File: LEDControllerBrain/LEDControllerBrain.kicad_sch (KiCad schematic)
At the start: 10 parts, among them J1 TB001-500-04BE, J2 TB001-500-04BE, J3 TB001-500-04BE, U1 NODEMCU-32S

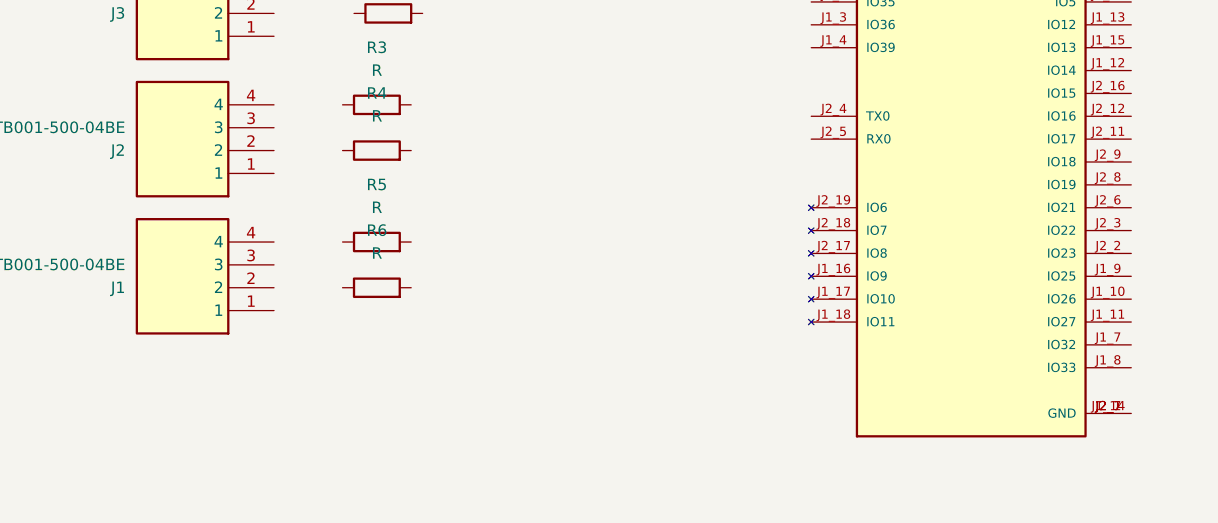
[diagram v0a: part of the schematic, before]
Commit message: add 24v support and reverse voltage protection
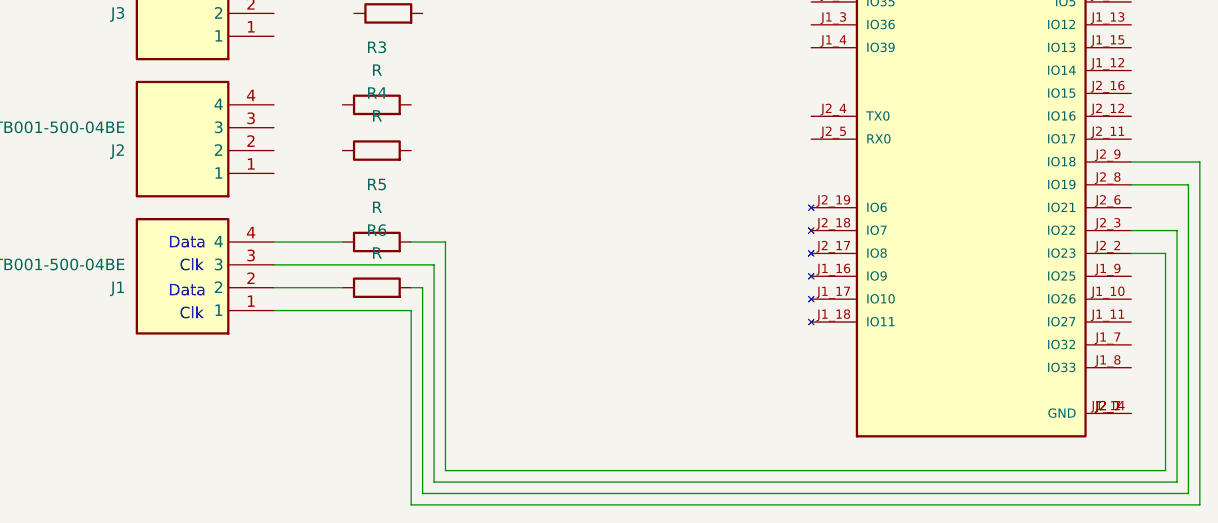
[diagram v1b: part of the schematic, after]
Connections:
- net at R6.1: now also J1.2
- net at R6.2: now also U1.J2_8 (IO19)
- net at J1.1: now also U1.J2_9 (IO18)
- net at J1.3: now also U1.J2_3 (IO22)
- net at J1.4: now also R5.1
- net at U1.J2_2 (IO23): now also R5.2
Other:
- note added: "Clk"
- note added: "Data"
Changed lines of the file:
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@@
 	(generator_version "8.0")
 	(paper "A4")
+	(wire
+		(pts
+			(xy 72.39 82.55) (xy 72.39 106.68)
+		)
+		(stroke
+			(width 0)
+			(type default)
+		)
+	)
+	(wire
+		(pts
+			(xy 157.48 71.12) (xy 149.86 71.12)
+		)
+		(stroke
+			(width 0)
+			(type default)
+		)
+	)
+	(wire
+		(pts
+			(xy 72.39 106.68) (xy 154.94 106.68)
+		)
+		(stroke
+			(width 0)
+			(type default)
+		)
+	)
+	(wire
+		(pts
+			(xy 156.21 107.95) (xy 156.21 73.66)
+		)
+		(stroke
+			(width 0)
+			(type default)
+		)
+	)
+	(wire
+		(pts
+			(xy 156.21 73.66) (xy 149.86 73.66)
+		)
+		(stroke
+			(width 0)
+			(type default)
+		)
+	)
+	(wire
+		(pts
+			(xy 73.66 105.41) (xy 153.67 105.41)
+		)
+		(stroke
+			(width 0)
+			(type default)
+		)
+	)
+	(wire
+		(pts
+			(xy 71.12 107.95) (xy 156.21 107.95)
+		)
+		(stroke
+			(width 0)
+			(type default)
+		)
+	)
+	(wire
+		(pts
+			(xy 72.39 82.55) (xy 54.61 82.55)
+		)
+		(stroke
+			(width 0)
+			(type default)
+		)
+	)
+	(wire
+		(pts
+			(xy 153.67 81.28) (xy 153.67 105.41)
+		)
+		(stroke
+			(width 0)
+			(type default)
+		)
+	)
+	(wire
+		(pts
+			(xy 154.94 78.74) (xy 154.94 106.68)
+		)
+		(stroke
+			(width 0)
+			(type default)
+		)
+	)
+	(wire
+		(pts
+			(xy 69.85 87.63) (xy 69.85 109.22)
+		)
+		(stroke
+			(width 0)
+			(type default)
+		)
+	)
+	(wire
+		(pts
+			(xy 149.86 81.28) (xy 153.67 81.28)
+		)
+		(stroke
+			(width 0)
+			(type default)
+		)
+	)
+	(wire
+		(pts
+			(xy 157.48 109.22) (xy 157.48 71.12)
+		)
+		(stroke
+			(width 0)
+			(type default)
+		)
+	)
+	(wire
+		(pts
+			(xy 54.61 80.01) (xy 62.23 80.01)
+		)
+		(stroke
+			(width 0)
+			(type default)
+		)
+	)
+	(wire
+		(pts
+			(xy 71.12 85.09) (xy 71.12 107.95)
+		)
+		(stroke
+			(width 0)
+			(type default)
+		)
+	)
+	(wire
+		(pts
+			(xy 69.85 85.09) (xy 71.12 85.09)
+		)
+		(stroke
+			(width 0)
+			(type default)
+		)
+	)
+	(wire
+		(pts
+			(xy 69.85 109.22) (xy 157.48 109.22)
+		)
+		(stroke
+			(width 0)
+			(type default)
+		)
+	)
+	(wire
+		(pts
+			(xy 54.61 87.63) (xy 69.85 87.63)
+		)
+		(stroke
+			(width 0)
+			(type default)
+		)
+	)
+	(wire
+		(pts
+			(xy 54.61 85.09) (xy 62.23 85.09)
+		)
+		(stroke
+			(width 0)
+			(type default)
+		)
+	)
+	(wire
+		(pts
+			(xy 154.94 78.74) (xy 149.86 78.74)
+		)
+		(stroke
+			(width 0)
+			(type default)
+		)
+	)
+	(wire
+		(pts
+			(xy 73.66 80.01) (xy 69.85 80.01)
+		)
+		(stroke
+			(width 0)
+			(type default)
+		)
+	)
+	(wire
+		(pts
+			(xy 73.66 105.41) (xy 73.66 80.01)
+		)
+		(stroke
+			(width 0)
+			(type default)
+		)
+	)
+	(text "Data"
+		(exclude_from_sim no)
+		(at 44.958 85.598 0)
+		(effects
+			(font
+				(size 1.27 1.27)
+			)
+		)
+	)
+	(text "Clk"
+		(exclude_from_sim no)
+		(at 45.466 88.138 0)
+		(effects
+			(font
+				(size 1.27 1.27)
+			)
+		)
+	)
+	(text "Clk"
+		(exclude_from_sim no)
+		(at 45.466 82.804 0)
+		(effects
+			(font
+				(size 1.27 1.27)
+			)
+		)
+	)
+	(text "Data"
+		(exclude_from_sim no)
+		(at 44.958 80.264 0)
+		(effects
+			(font
+				(size 1.27 1.27)
+			)
+		)
+	)
 	(symbol
 		(lib_id "Device:R")

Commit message: finished pdb
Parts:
- removed J3: TB001-500-04BE, TB00150004BE, symbol LEDController:TB001-500-04BE
- added R7: R, Resistor_THT:R_Axial_DIN0207_L6.3mm_D2.5mm_P10.16mm_Horizontal, symbol Device:R
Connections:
- net at R4.1: now also J1.4
- net at R4.2: now also U1.J2_14 (IO0)
- net at R6.2: now also U1.J2_9 (IO18); no longer U1.J2_8 (IO19)
- net at R1.1: now also J2.3
- net at R1.2: now also U1.J2_11 (IO17)
- net at R3.1: now also J2.1
- net at R3.2: now also U1.J2_13 (IO4)
- net at J1.1: now also U1.J2_8 (IO19); no longer U1.J2_9 (IO18)
- net at J1.3: now also R5.1; no longer U1.J2_3 (IO22)
- net at R2.1: now also J2.2
- net at R2.2: now also U1.J2_16 (IO15)
- net at U1.J2_10 (IO5): now also R7.2
- net at U1.J2_15 (IO2): now also R5.2
- net at U1.J2_2 (IO23): no longer R5.2
- net at J2.4: now also R7.1
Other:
- moved on the sheet: J1, J2, R1, R2, R3, R4, R5, R6, U1

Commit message: done
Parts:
- added IC1: 74LVC4245APW,118, LEDController:SOP65P640X110-24N, symbol LEDController:74LVC4245APW,118
- added J2: TB001-500-04BE, TB00150004BE, symbol LEDController:TB001-500-04BE
- added J5, J6: Conn_01x19_Pin, Connector_PinSocket_2.54mm:PinSocket_1x19_P2.54mm_Vertical, symbol Connector:Conn_01x19_Pin
- added J7: 647676-3, LEDController:TE_647676-3, symbol LEDController:647676-3
- added R10, R11, R8, R9: 100, Resistor_SMD:R_0603_1608Metric_Pad0.98x0.95mm_HandSolder, symbol Device:R
- added U2: DS18B20U, Package_SO:MSOP-8_3x3mm_P0.65mm, symbol Sensor_Temperature:DS18B20U
- R1: value R -> 1k; footprint Resistor_THT:R_Axial_DIN0207_L6.3mm_D2.5mm_P10.16mm_Horizontal -> Resistor_SMD:R_0603_1608Metric_Pad0.98x0.95mm_HandSolder
- R2: value R -> 10k; footprint Resistor_THT:R_Axial_DIN0207_L6.3mm_D2.5mm_P10.16mm_Horizontal -> Resistor_SMD:R_0603_1608Metric_Pad0.98x0.95mm_HandSolder
- R3, R4, R5, R6: value R -> 100; footprint Resistor_THT:R_Axial_DIN0207_L6.3mm_D2.5mm_P10.16mm_Horizontal -> Resistor_SMD:R_0603_1608Metric_Pad0.98x0.95mm_HandSolder
- R7: value R -> 4.7k; footprint Resistor_THT:R_Axial_DIN0207_L6.3mm_D2.5mm_P10.16mm_Horizontal -> Resistor_SMD:R_0603_1608Metric_Pad0.98x0.95mm_HandSolder
- renumbered J2 to J3, J1 to J4
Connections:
- net at R4.1: now also IC1.9 (A6); no longer J4.4
- net at R4.2: now also J3.2; no longer U1.J2_14 (IO0)
- net at R6.1: now also IC1.7 (A4); no longer J4.2
- net at R6.2: now also J3.4; no longer U1.J2_9 (IO18)
- net at J3.3: now also R5.2; no longer R1.1
- net 17: now reaches U1.J2_11 (IO17)
- net 17: now also IC1.16 (B5), J6.11 (Pin_11); no longer R1.2
- net at R3.1: now also IC1.10 (A7); no longer J3.1
- net at R3.2: now also J3.1; no longer U1.J2_13 (IO4)
- net at J4.1: now also R8.2; no longer U1.J2_8 (IO19)
- net at R5.1: now also IC1.8 (A5); no longer J4.3
- net 23: now reaches R2.1
- net 23: now also U1.J2_2 (IO23), J2.4, J6.2 (Pin_2); no longer J3.2
- net +3V3: now reaches R2.2
- net +3V3: now also U1.J1_1 (3.3V), IC1.23 (VCC(B)_1), IC1.24 (VCC(B)_2), J5.1 (Pin_1); no longer U1.J2_16 (IO15)
- net 26: now reaches U1.J1_10 (IO26)
- net 26: now also J5.10 (Pin_10)
- net 27: now reaches U1.J1_11 (IO27)
- net 27: now also J5.11 (Pin_11)
- net 14: now reaches U1.J1_12 (IO14)
- net 14: now also J5.12 (Pin_12)
- net 12: now reaches U1.J1_13 (IO12)
- net 12: now also J5.13 (Pin_13)
- net GND: now reaches U1.J1_14 (GND), U1.J2_1 (GND), U1.J2_7 (GND)
- net GND: now also IC1.11 (GND_1), IC1.12 (GND_2), IC1.13 (GND_3), IC1.2 (DIR), IC1.22 (~{OE}), J2.1, J2.3, J5.14 (Pin_14), J6.1 (Pin_1), J6.7 (Pin_7), J7.2, U2.4 (GND)
- net 13: now reaches U1.J1_15 (IO13)
- net 13: now also J5.15 (Pin_15)
- net 9: now reaches U1.J1_16 (IO9)
- net 9: now also J5.16 (Pin_16)
- net 10: now reaches U1.J1_17 (IO10)
- net 10: now also J5.17 (Pin_17)
- net 11: now reaches U1.J1_18 (IO11)
- net 11: now also J5.18 (Pin_18)
- net +5V: now reaches U1.J1_19 (5V)
- net +5V: now also R7.1, IC1.1 (VCC(A)), J5.19 (Pin_19), J7.3, U2.8 (V_{DD})
- net EN: now reaches U1.J1_2 (EN)
- net EN: now also J5.2 (Pin_2)
- net 36: now reaches U1.J1_3 (IO36)
- net 36: now also J5.3 (Pin_3)
- net 39: now reaches U1.J1_4 (IO39)
- net 39: now also J5.4 (Pin_4)
- net 34: now reaches U1.J1_5 (IO34)
- net 34: now also J5.5 (Pin_5)
- net 35: now reaches U1.J1_6 (IO35)
- net 35: now also J5.6 (Pin_6)
- net 32: now reaches U1.J1_7 (IO32)
- net 32: now also J5.7 (Pin_7)
- net 33: now reaches U1.J1_8 (IO33)
- net 33: now also J5.8 (Pin_8)
- net 25: now reaches U1.J1_9 (IO25)
- net 25: now also R7.2, J5.9 (Pin_9), U2.1 (DQ)
- net 5: now reaches U1.J2_10 (IO5)
- net 5: now also IC1.15 (B6), J6.10 (Pin_10); no longer R7.2
- net 16: now reaches U1.J2_12 (IO16)
- net 16: now also IC1.17 (B4), J6.12 (Pin_12)
- net 2: now reaches U1.J2_15 (IO2)
- net 2: now also IC1.19 (B2), J6.15 (Pin_15); no longer R5.2
- net 8: now reaches U1.J2_17 (IO8)
- net 8: now also J6.17 (Pin_17)
- net 7: now reaches U1.J2_18 (IO7)
- net 7: now also J6.18 (Pin_18)
- net 6: now reaches U1.J2_19 (IO6)
- net 6: now also J6.19 (Pin_19)
- net 22: now reaches U1.J2_3 (IO22)
- net 22: now also IC1.14 (B7), J6.3 (Pin_3)
- net 1: now reaches U1.J2_4 (TX0)
- net 1: now also J6.4 (Pin_4)
- net 3: now reaches U1.J2_5 (RX0)
- net 3: now also J6.5 (Pin_5)
- net 21: now reaches U1.J2_6 (IO21)
- net 21: now also R1.2, J6.6 (Pin_6)
- new net: IC1.6 (A3), R8.1
- new net: IC1.3 (A0), R11.1
- new net: IC1.4 (A1), R10.1
- new net: IC1.5 (A2), R9.1
- new net: J4.2, R9.2
- new net: J4.3, R10.2
- new net: J4.4, R11.2
- new net 0: J6.14 (Pin_14), U1.J2_14 (IO0)
- new net 15: J6.16 (Pin_16), U1.J2_16 (IO15)
- new net 18: IC1.20 (B1), J6.9 (Pin_9), U1.J2_9 (IO18)
- new net 19: IC1.21 (B0), J6.8 (Pin_8), U1.J2_8 (IO19)
- new net 4: IC1.18 (B3), J6.13 (Pin_13), U1.J2_13 (IO4)
- new net Relay Controll: J2.2, J7.1, R1.1
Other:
- note added: "2 , 4 ,16, 17 , 5"
- note added: "NC"
- note added: "Pins [0,6,7,8,9,10,11,14,15,24,28,29,30,31,32 Cannot be used"
- moved on the sheet: J3, J4

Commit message: generate outputs
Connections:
- net +3V3: now also R2.1; no longer R2.2
- net 23: now also R2.2; no longer R2.1
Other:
- title: (none) -> LED Control Board
- moved on the sheet: R2
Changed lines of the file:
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@@
 	(generator_version "9.0")
 	(paper "A4")
+	(title_block
+		(title "LED Control Board")
+		(date "2025-04-18")
+		(rev "01")
+	)
 	(text "Pins [0,6,7,8,9,10,11,14,15,24,28,29,30,31,32 Cannot be used"
 		(exclude_from_sim no)
@@
 	(wire
 		(pts
-			(xy 142.24 46.99) (xy 142.24 49.53)
+			(xy 148.59 48.26) (xy 148.59 46.99)
 		)
 		(stroke
@@
 	(wire
 		(pts
-			(xy 156.21 66.04) (xy 157.48 66.04)
+			(xy 152.4 66.04) (xy 157.48 66.04)
 		)
 		(stroke
@@
 		)
 	)
+	(wire
+		(pts
+			(xy 123.19 63.5) (xy 123.19 62.23)
+		)
+		(stroke
+			(width 0)
+			(type default)
+		)
+	)
 	(bus
 		(pts
@@
 		)
 	)
+	(wire
+		(pts
+			(xy 148.59 48.26) (xy 142.24 48.26)
+		)
+		(stroke
+			(width 0)
+			(type default)
+		)
+	)
 	(bus
 		(pts
@@
 		)
 	)
+	(wire
+		(pts
+			(xy 123.19 53.34) (xy 123.19 54.61)
+		)
+		(stroke
+			(width 0)
+			(type default)
+		)
+	)
 	(bus
 		(pts
@@
 		)
 	)
+	(wire
+		(pts
+			(xy 88.9 113.03) (xy 88.9 115.57)
+		)
+		(stroke
+			(width 0)
+			(type default)
+		)
+	)
 	(bus
 		(pts
@@
 	(wire
 		(pts
+			(xy 142.24 48.26) (xy 142.24 46.99)
+		)
+		(stroke
+			(width 0)
+			(type default)
+		)
+	)
+	(wire
+		(pts
 			(xy 147.32 115.57) (xy 157.48 115.57)
 		)
@@
 	(wire
 		(pts
-			(xy 156.21 71.12) (xy 157.48 71.12)
+			(xy 152.4 71.12) (xy 157.48 71.12)
 		)
 		(stroke
@@
 	(wire
 		(pts
-			(xy 123.19 72.39) (xy 123.19 71.12)
-		)
-		(stroke
-			(width 0)
-			(type default)
-		)
-	)
-	(wire
-		(pts
 			(xy 156.21 113.03) (xy 156.21 109.22)
 		)
@@
 	(symbol
 		(lib_id "power:+5V")
-		(at 142.24 49.53 180)
+		(at 148.59 46.99 0)
 		(unit 1)
 		(exclude_from_sim no)
@@
 		(dnp no)
 		(property "Reference" "#PWR04"
-			(at 142.24 45.72 0)
+			(at 148.59 50.8 0)
 			(effects
 				(font
@@
 		)
 		(property "Value" "+5V"
-			(at 144.78 51.308 0)
+			(at 146.05 45.212 0)
 			(effects
 				(font
@@
 		)
 		(property "Footprint" ""
-			(at 142.24 49.53 0)
+			(at 148.59 46.99 0)
 			(effects
 				(font
@@
 		)
 		(property "Datasheet" ""
-			(at 142.24 49.53 0)
+			(at 148.59 46.99 0)
 			(effects
 				(font
@@
 		)
 		(property "Description" "Power symbol creates a global label with name \"+5V\""
-			(at 142.24 49.53 0)
+			(at 148.59 46.99 0)
 			(effects
 				(font
@@
 	(symbol
 		(lib_id "power:+5V")
-		(at 88.9 115.57 90)
+		(at 88.9 113.03 0)
 		(unit 1)
 		(exclude_from_sim no)
@@
 		(on_board yes)
 		(dnp no)
-		(fields_autoplaced yes)
 		(property "Reference" "#PWR010"
-			(at 92.71 115.57 0)
+			(at 88.9 116.84 0)
 			(effects
 				(font
@@
 		)
 		(property "Value" "+5V"
-			(at 85.09 115.5699 90)
+			(at 83.566 111.76 0)
 			(effects
 				(font
@@
 		)
 		(property "Footprint" ""
-			(at 88.9 115.57 0)
+			(at 88.9 113.03 0)
 			(effects
 				(font
@@
 		)
 		(property "Datasheet" ""
-			(at 88.9 115.57 0)
+			(at 88.9 113.03 0)
 			(effects
 				(font
@@
 		)
 		(property "Description" "Power symbol creates a global label with name \"+5V\""
-			(at 88.9 115.57 0)
+			(at 88.9 113.03 0)
 			(effects
 				(font
@@
 	(symbol
 		(lib_id "power:GND")
-		(at 149.86 102.87 90)
+		(at 149.86 102.87 0)
+		(mirror y)
 		(unit 1)
 		(exclude_from_sim no)
@@
 		(on_board yes)
 		(dnp no)
-		(fields_autoplaced yes)
 		(property "Reference" "#PWR09"
-			(at 156.21 102.87 0)
+			(at 149.86 109.22 0)
 			(effects
 				(font
@@
 		)
 		(property "Value" "GND"
-			(at 153.67 102.8699 90)
+			(at 149.8599 106.68 90)
 			(effects
 				(font
@@
 	(symbol
 		(lib_id "power:GND")
-		(at 156.21 71.12 270)
+		(at 152.4 71.12 0)
 		(unit 1)
 		(exclude_from_sim no)
@@
 		(fields_autoplaced yes)
 		(property "Reference" "#PWR06"
-			(at 149.86 71.12 0)
+			(at 152.4 77.47 0)
 			(effects
 				(font
@@
 		)
 		(property "Value" "GND"
-			(at 152.4 71.1199 90)
+			(at 154.94 72.3899 0)
 			(effects
 				(font
 					(size 1.27 1.27)
 				)
-				(justify right)
+				(justify left)
 			)
 		)
 		(property "Footprint" ""
-			(at 156.21 71.12 0)
+			(at 152.4 71.12 0)
 			(effects
 				(font
@@
 		)
 		(property "Datasheet" ""
-			(at 156.21 71.12 0)
+			(at 152.4 71.12 0)
 			(effects
 				(font
@@
 		)
 		(property "Description" "Power symbol creates a global label with name \"GND\" , ground"
-			(at 156.21 71.12 0)
+			(at 152.4 71.12 0)
 			(effects
 				(font
@@
 	(symbol
 		(lib_id "Device:R")
-		(at 123.19 67.31 0)
+		(at 123.19 58.42 0)
 		(unit 1)
 		(exclude_from_sim no)
@@
 		(fields_autoplaced yes)
 		(property "Reference" "R2"
-			(at 125.73 66.0399 0)
+			(at 125.73 57.1499 0)
 			(effects
 				(font
@@
 		)
 		(property "Value" "10k"
-			(at 125.73 68.5799 0)
+			(at 125.73 59.6899 0)
 			(effects
 				(font
@@
 		)
 		(property "Footprint" "Resistor_SMD:R_0603_1608Metric_Pad0.98x0.95mm_HandSolder"
-			(at 121.412 67.31 90)
+			(at 121.412 58.42 90)
 			(effects
 				(font
@@
 		)
 		(property "Datasheet" "~"
-			(at 123.19 67.31 0)
+			(at 123.19 58.42 0)
 			(effects
 				(font
@@
 		)
 		(property "Description" "Resistor"
-			(at 123.19 67.31 0)
+			(at 123.19 58.42 0)
 			(effects
 				(font
@@
 	(symbol
 		(lib_id "power:GND")
-		(at 156.21 66.04 270)
+		(at 152.4 66.04 0)
 		(unit 1)
 		(exclude_from_sim no)
@@
 		(fields_autoplaced yes)
 		(property "Reference" "#PWR05"
-			(at 149.86 66.04 0)
+			(at 152.4 72.39 0)
 			(effects
 				(font
@@
 		)
 		(property "Value" "GND"
-			(at 152.4 66.0399 90)
+			(at 154.94 67.3099 0)
 			(effects
 				(font
 					(size 1.27 1.27)
 				)
-				(justify right)
+				(justify left)
 			)
 		)
 		(property "Footprint" ""
-			(at 156.21 66.04 0)
+			(at 152.4 66.04 0)
 			(effects
 				(font
@@
 		)
 		(property "Datasheet" ""
-			(at 156.21 66.04 0)
+			(at 152.4 66.04 0)
 			(effects
 				(font
@@
 		)
 		(property "Description" "Power symbol creates a global label with name \"GND\" , ground"
-			(at 156.21 66.04 0)
+			(at 152.4 66.04 0)
 			(effects
 				(font
@@
 	(symbol
 		(lib_id "power:GND")
-		(at 92.71 102.87 90)
+		(at 92.71 102.87 0)
 		(unit 1)
 		(exclude_from_sim no)
@@
 		(on_board yes)
 		(dnp no)
-		(fields_autoplaced yes)
 		(property "Reference" "#PWR08"
-			(at 99.06 102.87 0)
+			(at 92.71 109.22 0)
 			(effects
 				(font
@@
 		)
 		(property "Value" "GND"
-			(at 96.52 102.8699 90)
+			(at 87.376 105.41 0)
 			(effects
 				(font
 					(size 1.27 1.27)
 				)
-				(justify right)
+				(justify left)
 			)
 		)
@@
 	(symbol
 		(lib_id "power:+3V3")
-		(at 123.19 72.39 180)
+		(at 123.19 53.34 0)
 		(unit 1)
 		(exclude_from_sim no)
@@
 		(on_board yes)
 		(dnp no)
-		(fields_autoplaced yes)
 		(property "Reference" "#PWR07"
-			(at 123.19 68.58 0)
+			(at 123.19 57.15 0)
 			(effects
 				(font
@@
 		)
 		(property "Value" "+3V3"
-			(at 123.19 77.47 0)
+			(at 116.84 52.832 0)
 			(effects
 				(font
 					(size 1.27 1.27)
 				)
+				(justify left)
 			)
 		)
 		(property "Footprint" ""
-			(at 123.19 72.39 0)
+			(at 123.19 53.34 0)
 			(effects
 				(font
@@
 		)
 		(property "Datasheet" ""
-			(at 123.19 72.39 0)
+			(at 123.19 53.34 0)
 			(effects
 				(font
@@
 		)
 		(property "Description" "Power symbol creates a global label with name \"+3V3\""
-			(at 123.19 72.39 0)
+			(at 123.19 53.34 0)
 			(effects
 				(font
